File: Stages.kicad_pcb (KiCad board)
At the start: 2 copper layers, 69 x 100 mm, 223 parts, among them IC1 TLC59281, IC10 MCP6002, IC11 LM4040DBZ-2.5, IC12 TL074, IC13 TL074, IC14 TL074, IC2 R-78E3.3-0.5, IC3 4051, IC4 DAC8168, IC5 STM32F373RBTx, IC6 4051, IC7 LD2981ABU33, IC8 MCP6002, IC9 MCP6002, J1 -8.1V to 8.1V, J10 WQP-PJ301M-12_JACK, J11 WQP-PJ301M-12_JACK, J12 WQP-PJ301M-12_JACK, J13 -8.1V to 8.1V, J14 -8.1V to 8.1V, J15 -8.1V to 8.1V, J16 -8.1V to 8.1V, J17 -8.1V to 8.1V, J18 -8.1V to 8.1V, J2 -8.1V to 8.1V, J3 -8.1V to 8.1V, J4 -8.1V to 8.1V, J5 -8.1V to 8.1V, J6 -8.1V to 8.1V, J7 WQP-PJ301M-12_JACK, J8 WQP-PJ301M-12_JACK, J9 WQP-PJ301M-12_JACK, Q1 8MHz, Q2 MMBT3904, Q3 MMBT3904, Q4 MMBT3904, Q5 MMBT3904, Q6 MMBT3904, Q7 MMBT3904, SW1 SW_Push_4pin, SW2 SW_Push_4pin, SW3 SW_Push_4pin, SW4 SW_Push_4pin, SW5 SW_Push_4pin, SW6 SW_Push_4pin

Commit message: Routing Complete
time to tidy up connections
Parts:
- moved R7 10.2 mm to (153.9, 65.3), turned to 0 degrees
- moved R5 9.27 mm to (161.8, 64.8), turned to 180 degrees
- moved R10 8.70 mm to (109.5, 65.0), turned to 0 degrees
- moved D1 5.85 mm to (158.0, 79.8)
- moved R11 5.33 mm to (107.2, 71.4)
- moved D2 4.83 mm to (158.0, 85.1)
- moved C6 4.72 mm to (133.3, 84.1), turned to 270 degrees
- moved R18 3.53 mm to (106.7, 103.1), turned to 180 degrees
- moved JP6 2.03 mm to (131.1, 97.5)
- moved C10 1.27 mm to (140.5, 100.8), turned to 180 degrees
- moved C9 1.27 mm to (134.6, 100.8), turned to 0 degrees
- moved R1 1.19 mm to (140.0, 76.9)
- moved C11 1.02 mm to (130.6, 101.3)
- moved C14 1.02 mm to (128.0, 101.3)
- moved R41 0.25 mm to (102.6, 128.8)
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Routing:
- net NORMALIZATION_PROBE: track 0.00 -> 161.7 mm, vias 0 -> 22
- net GATE_1: track 0.00 -> 112.6 mm, vias 0 -> 2
- net GATE_2: track 0.00 -> 110.1 mm, vias 0 -> 2
- net +3V3: track 61.9 -> 167.5 mm, vias 2 -> 6
- net VREF_BIAS: track 0.00 -> 104.2 mm, vias 0 -> 15
- net GATE_3: track 0.00 -> 90.2 mm, vias 0 -> 2
- net GATE_4: track 0.00 -> 88.9 mm, vias 0 -> 2
- net Net-(IC3-Pad5): track 0.00 -> 79.3 mm, vias 0 -> 7
- net ADC_CV_1: track 5.26 -> 74.5 mm, vias 0 -> 3
- net GATE_5: track 0.00 -> 68.0 mm, vias 0 -> 2
- net Net-(IC6-Pad1): track 0.00 -> 67.8 mm, vias 0 -> 1
- net GATE_6: track 0.00 -> 67.2 mm, vias 0 -> 2
- net Net-(IC3-Pad2): track 0.00 -> 67.0 mm, vias 0 -> 5
- net STAGE_LED_1: track 0.00 -> 67.0 mm, vias 0 -> 2
- net SW_MODE_1: track 0.00 -> 64.8 mm, vias 0 -> 1
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- removed copper zone on B.Cu, net 4051GND

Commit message: DRC Complete
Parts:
- moved C43 20.5 mm to (122.2, 109.7), turned to 0 degrees
- moved R48 15.1 mm to (118.4, 109.0), turned to 180 degrees
- moved C22 2.84 mm to (128.5, 109.0), turned to 0 degrees
- moved R18 1.37 mm to (108.0, 103.6)
- moved R40 1.05 mm to (122.2, 112.3), turned to 180 degrees
- moved C18 1.01 mm to (125.2, 111.0), turned to 90 degrees
- moved R71 0.25 mm to (138.2, 140.0)
- moved C49 0.25 mm to (165.4, 128.8)
- moved R72 0.25 mm to (135.4, 140.0)
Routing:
- net 4051GND: track 4.42 -> 161.2 mm, vias 0 -> 82
- net STAGE_LED_3: track 0.00 -> 23.6 mm, vias 0 -> 2
- net VREF_BIAS: track 104.2 -> 84.8 mm, vias 15 -> 13
- net +3V3: track 167.5 -> 183.7 mm
- net Net-(C40-Pad1): track 0.00 -> 4.99 mm
- net VEE: track 156.1 -> 159.4 mm
- net SW_MODE_4: track 30.1 -> 32.8 mm
- net SW_MODE_6: track 35.9 -> 38.2 mm
- net Net-(J10-PadP$1): track 10.4 -> 12.4 mm
- net ADC_SHAPE: track 20.0 -> 21.8 mm
- net SW_MODE_2: track 52.0 -> 53.6 mm
- net ADC_CV_5: track 62.1 -> 60.5 mm
- net DAC_2: track 41.2 -> 42.7 mm
- net +3V3_A: track 317.1 -> 318.5 mm
- net SW_MODE_5: track 25.6 -> 26.8 mm
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- added copper zone on B.Cu, net 4051GND
- added copper zone on F.Cu, net 4051GND

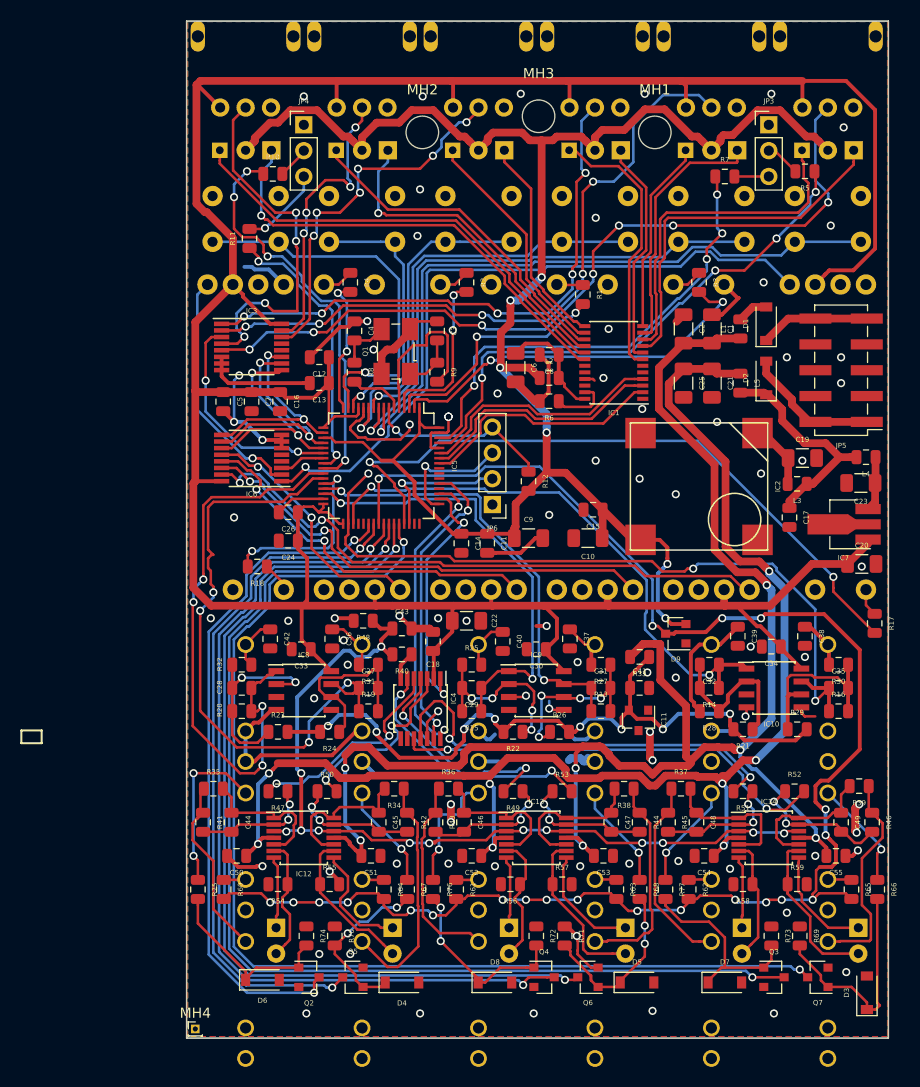
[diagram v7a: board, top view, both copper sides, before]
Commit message: Removed to plane and re-routed
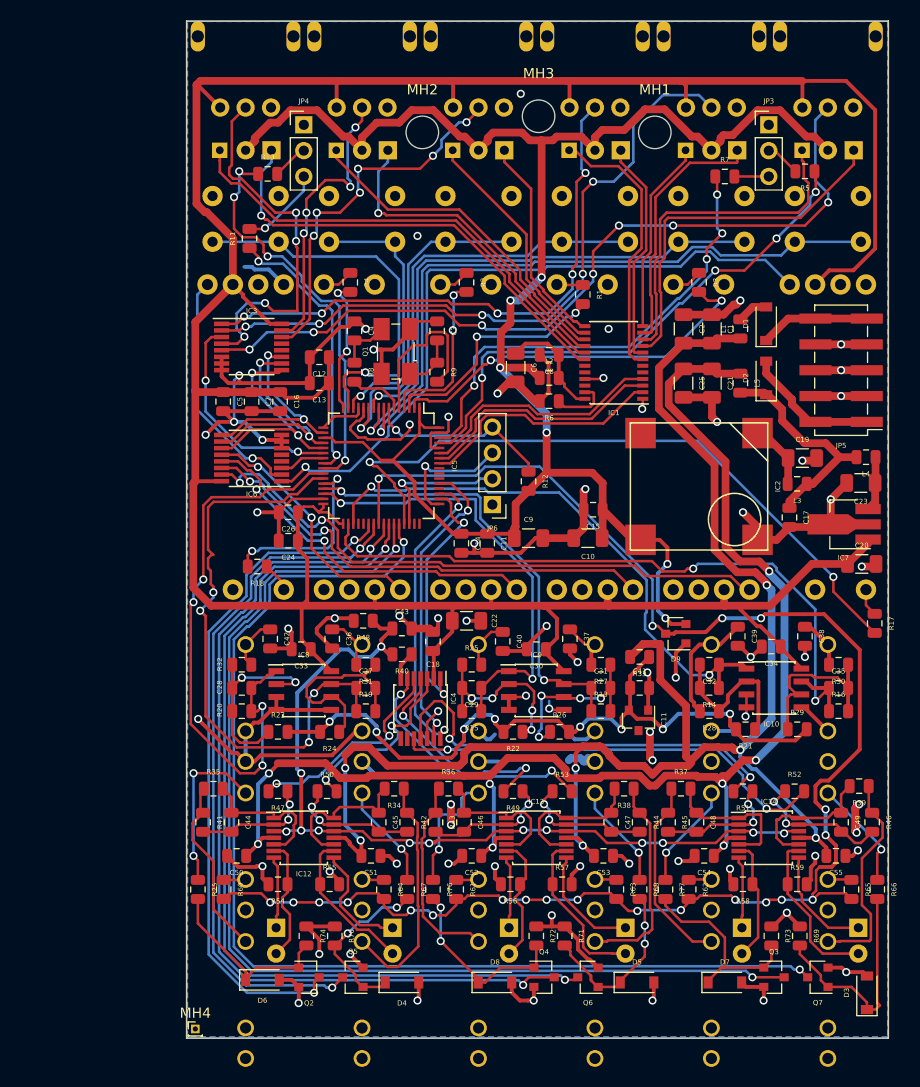
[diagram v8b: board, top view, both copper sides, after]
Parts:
- moved R10 0.51 mm to (109.0, 65.0)
- moved C27 0.25 mm to (118.6, 115.6)
- moved R19 0.25 mm to (118.6, 117.9)
- moved R31 0.25 mm to (118.6, 113.3)
- moved R21 0.25 mm to (156.0, 119.6)
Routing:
- net 4051GND: track 161.2 -> 341.6 mm, vias 82 -> 69
- net ADC_CV_1: track 73.6 -> 67.9 mm, vias 3 -> 2
- net Net-(C27-Pad2): track 17.9 -> 19.9 mm
- net ADC_CV_5: track 60.5 -> 58.7 mm
- net +3V3: track 183.7 -> 185.3 mm
- net Net-(IC3-Pad4): track 36.2 -> 37.0 mm
- net Net-(JP4-Pad2): track 3.16 -> 3.74 mm
- removed copper zone on F.Cu, net 4051GND
